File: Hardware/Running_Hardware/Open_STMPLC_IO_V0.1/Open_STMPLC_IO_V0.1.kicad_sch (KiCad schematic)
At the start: 73 parts, among them J1 Screw_Terminal_01x02, J2 Screw_Terminal_01x02, J3 Screw_Terminal_01x02, J4 Screw_Terminal_01x02, J5 Screw_Terminal_01x04, Q1 SUD50P06, Q2 AO3400A, SW1 SW_SPDT, SW2 SW_SPDT, SW3 SW_DIP_x02, SW4 SW_SPDT, U10 MAX31865xTP, U11 MAX31856, U12 6N137, U3 TPS1H200A, U7 TPS26600PWP, U8 UCC23513

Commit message: IO board changes
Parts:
- removed C1: 100nF, symbol Device:C_Small
- removed C10: 620nF, symbol Device:C_Small
- removed C11, C14, C6: 10nF, Capacitor_SMD:C_0603_1608Metric_Pad1.08x0.95mm_HandSolder, symbol Device:C_Small
- removed C12, C13, C15, C4, C5, C7: 100nF, Capacitor_SMD:C_0603_1608Metric_Pad1.08x0.95mm_HandSolder, symbol Device:C_Small
- removed C2: 10uF, symbol Device:C_Small
- removed C8: 1uF, symbol Device:C_Small
- removed C9: 2.2uF, symbol Device:C_Small
- removed D1, D2, D6, D7: SS54, symbol Device:D_Schottky_Small
- removed D10, D3, D5: SMAJ33CA, Diode_SMD:D_SMA, symbol Diode:SMAJ33CA
- removed D4: BZT52C12, symbol Device:D_Zener_Small
- removed FB1, FB2: 120R@100MHz, symbol Device:FerriteBead_Small
- removed J1, J2, J4: Screw_Terminal_01x02, symbol Connector:Screw_Terminal_01x02
- removed J5: Screw_Terminal_01x04, symbol Connector:Screw_Terminal_01x04
- removed Q1: SUD50P06, Package_TO_SOT_SMD:TO-252-3_TabPin2, symbol Transistor_FET:Q_PMOS_GDS
- removed Q2: AO3400A, Package_TO_SOT_SMD:SOT-23, symbol Transistor_FET:AO3400A
- removed R1, R14: 10K, symbol Device:R_Small
- removed R10: 1K, symbol Device:R_Small
- removed R11: 470R, symbol Device:R_Small
- removed R12, R13: 150R, Resistor_SMD:R_0603_1608Metric_Pad0.98x0.95mm_HandSolder, symbol Device:R_Small
- removed R15: 100K, symbol Device:R_Small
- removed R16, R3: 10K, Resistor_SMD:R_0603_1608Metric_Pad0.98x0.95mm_HandSolder, symbol Device:R_Small
- removed R17, R19, R20: 4.7K, Resistor_SMD:R_0603_1608Metric_Pad0.98x0.95mm_HandSolder, symbol Device:R_Small
- removed R18: 15K, symbol Device:R_Small
- removed R2: 47R, symbol Device:R_Small
- removed R21, R23, R24: 2.2K, Resistor_SMD:R_0603_1608Metric_Pad0.98x0.95mm_HandSolder, symbol Device:R_Small
- removed R26: 400R, Resistor_SMD:R_0603_1608Metric_Pad0.98x0.95mm_HandSolder, symbol Device:R_Small
- removed R28: 4K, Resistor_SMD:R_0603_1608Metric_Pad0.98x0.95mm_HandSolder, symbol Device:R_Small
- removed R4: 1K, Resistor_SMD:R_0603_1608Metric_Pad0.98x0.95mm_HandSolder, symbol Device:R_Small
- removed R5: 715K, Resistor_SMD:R_0603_1608Metric_Pad0.98x0.95mm_HandSolder, symbol Device:R_Small
- removed R6: 20K, Resistor_SMD:R_0603_1608Metric_Pad0.98x0.95mm_HandSolder, symbol Device:R_Small
- removed R7: 30.1K, Resistor_SMD:R_0603_1608Metric_Pad0.98x0.95mm_HandSolder, symbol Device:R_Small
- removed R8: 11.8K, Resistor_SMD:R_0603_1608Metric_Pad0.98x0.95mm_HandSolder, symbol Device:R_Small
- removed R9: 33.2K, Resistor_SMD:R_0603_1608Metric_Pad0.98x0.95mm_HandSolder, symbol Device:R_Small
- removed SW1, SW2, SW4: SW_SPDT, symbol Switch:SW_SPDT
- removed SW3: SW_DIP_x02, symbol Switch:SW_DIP_x02
- removed U10: MAX31865xTP, Package_DFN_QFN:TQFN-20-1EP_5x5mm_P0.65mm_EP3.25x3.25mm, symbol Sensor_Temperature:MAX31865xTP
- removed U11: MAX31856, Package_SO:TSSOP-14_4.4x5mm_P0.65mm, symbol Sensor_Temperature:MAX31856
- removed U3: TPS1H200A, Package_SO:HVSSOP-8-1EP_3x3mm_P0.65mm_EP1.57x1.89mm_ThermalVias, symbol TPS1H200A:TPS1H200A
- removed U7: TPS26600PWP, Package_SO:HTSSOP-16-1EP_4.4x5mm_P0.65mm_EP3.4x5mm_Mask2.66x2.46mm_ThermalVias, symbol Power_Management:TPS26600PWP
- removed U8: UCC23513, Package_SO:SSO-6_6.8x4.6mm_P1.27mm_Clearance8mm, symbol UCC23153:UCC23513
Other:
- added sheet DIG_HS_OUT_1 (untitled.kicad_sch)
- added sheet DIG_OUT (DIG_OUT.kicad_sch)
- added sheet Temp_Sensor (Temp_Sensor.kicad_sch)
- note removed: "2/3W"
- note removed: "2/4W"
- note removed: "2W"
- note removed: "3W"
- note removed: "PT100"
- note removed: "PT1000"

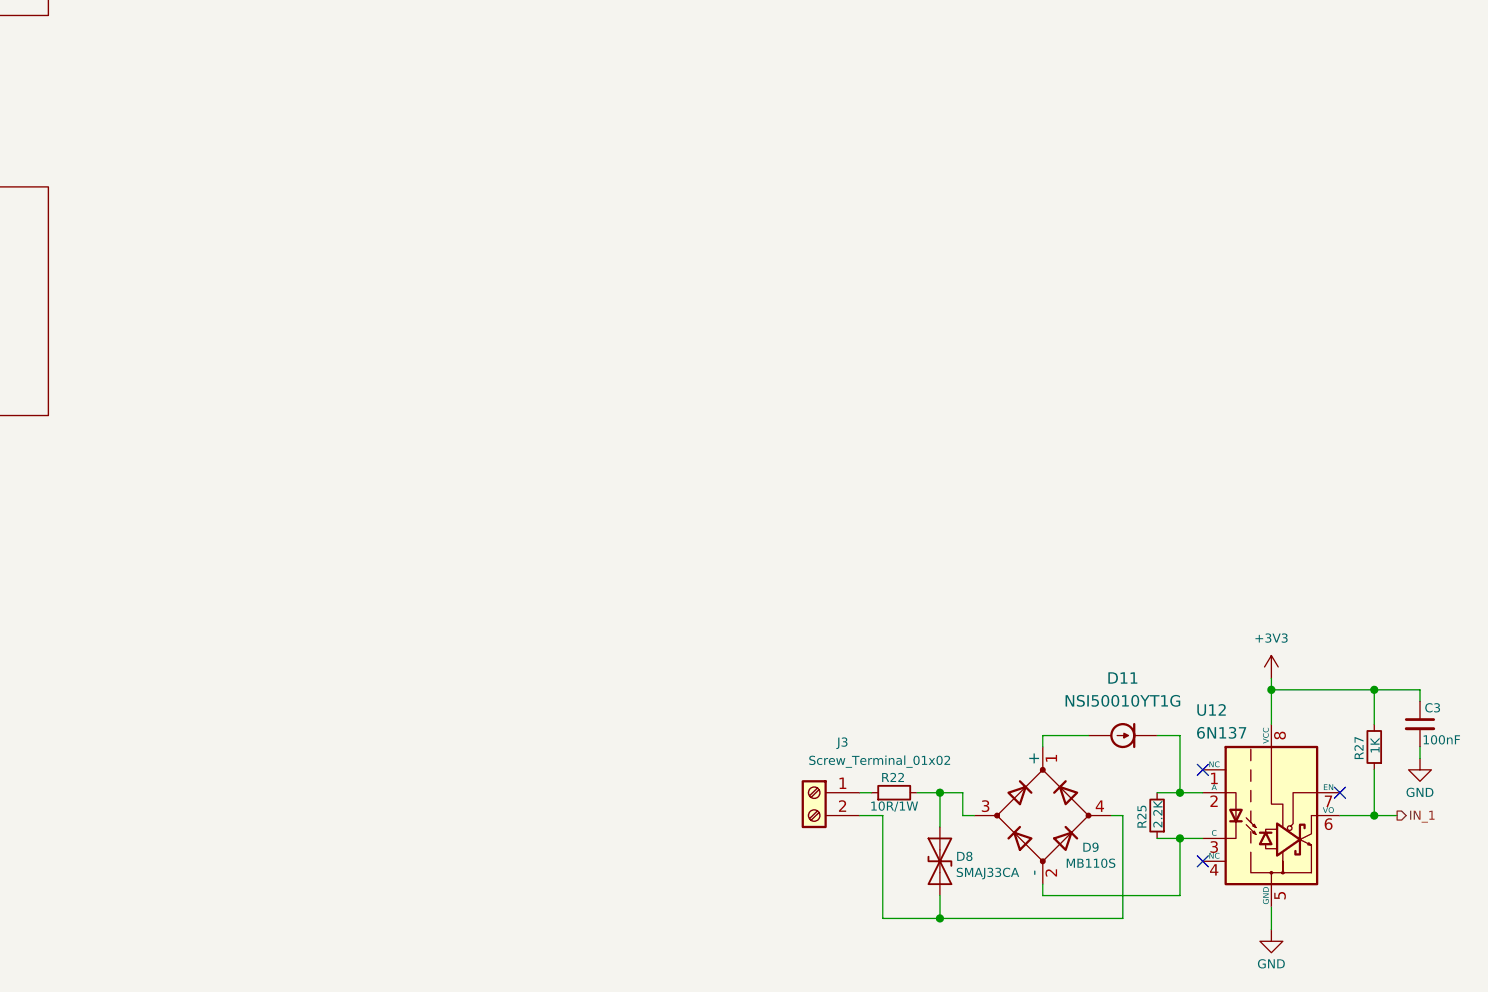
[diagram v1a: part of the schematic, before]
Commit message: IO board schematic changes
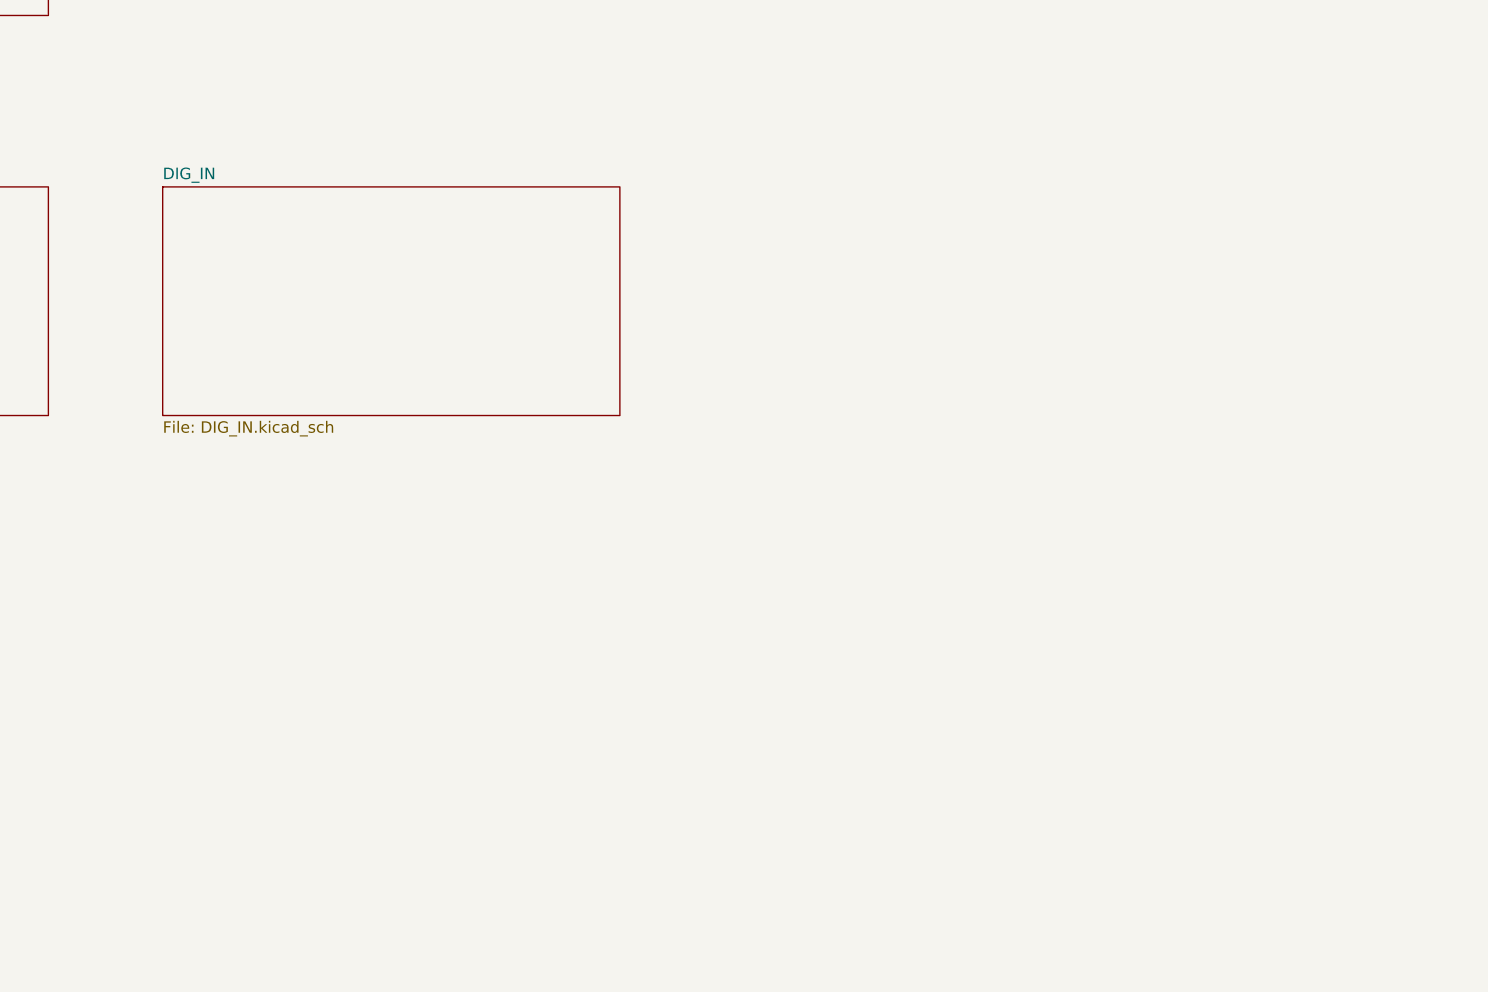
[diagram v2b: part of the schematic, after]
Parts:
- removed C3: 100nF, symbol Device:C_Small
- removed D11: NSI50010YT1G, Diode_SMD:D_SOD-123, symbol Device:D_Current-regulator
- removed D8: SMAJ33CA, Diode_SMD:D_SMA, symbol Diode:SMAJ33CA
- removed D9: MB110S, Package_TO_SOT_SMD:TO-269AA, symbol Device:D_Bridge_+-AA
- removed J3: Screw_Terminal_01x02, symbol Connector:Screw_Terminal_01x02
- removed R22: 10R/1W, Resistor_SMD:R_0603_1608Metric_Pad0.98x0.95mm_HandSolder, symbol Device:R_Small
- removed R25: 2.2K, Resistor_SMD:R_0603_1608Metric_Pad0.98x0.95mm_HandSolder, symbol Device:R_Small
- removed R27: 1K, Resistor_SMD:R_0603_1608Metric_Pad0.98x0.95mm_HandSolder, symbol Device:R_Small
- removed U12: 6N137, Package_DIP:DIP-8_W7.62mm, symbol Isolator:6N137
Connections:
- no-connect marks 3 -> 0
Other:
- added sheet DIG_IN (DIG_IN.kicad_sch)

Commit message: Digital IO completion
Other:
- removed sheet DIG_IN
- added sheet DIG_HS_OUT_2 (DIG_HS_OUT_2.kicad_sch)
- added sheet DIG_HS_OUT_3 (DIG_HS_OUT_3.kicad_sch)
- added sheet DIG_HS_OUT_4 (DIG_HS_OUT_4.kicad_sch)
- added sheet DIG_IN_GRP1 (DIG_IN_GRP1.kicad_sch)
- added sheet DIG_IN_GRP2 (DIG_IN_GRP2.kicad_sch)
- added sheet DIG_IN_GRP3 (DIG_IN_GRP3.kicad_sch)
- sheet DIG_HS_OUT_1: file untitled.kicad_sch -> DIG_HS_OUT_1.kicad_sch

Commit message: Analog out section
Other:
- added sheet ANALOG_IN (ANALOG_IN.kicad_sch)
- added sheet ANALOG_OUT (ANALOG_OUT.kicad_sch)
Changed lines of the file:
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@@
+	)
+	(sheet
+		(at 114.3 170.18)
+		(size 50.8 25.4)
+		(exclude_from_sim no)
+		(in_bom yes)
+		(on_board yes)
+		(dnp no)
+		(stroke
+			(width 0.1524)
+			(type solid)
+		)
+		(fill
+			(color 255 255 194 1.0000)
+		)
+		(property "Sheetname" "ANALOG_IN"
+			(at 114.554 173.99 0)
+			(effects
+				(font
+					(size 2 2)
+					(thickness 0.4)
+					(bold yes)
+				)
+				(justify left bottom)
+			)
+		)
+		(property "Sheetfile" "ANALOG_IN.kicad_sch"
+			(at 114.3 196.1646 0)
+			(effects
+				(font
+					(size 1.27 1.27)
+				)
+				(justify left top)
+			)
+		)
+		(instances
+			(project "Open_STMPLC_IO_V0.1"
+				(path "/4d6787b6-1f4f-4098-b70b-d936e584350b"
+					(page "11")
+				)
+			)
+		)
 	)
 	(sheet
@@
 				)
 			)
+		)
+	)
+	(sheet
+		(at 50.8 170.18)
+		(size 50.8 25.4)
+		(exclude_from_sim no)
+		(in_bom yes)
+		(on_board yes)
+		(dnp no)
+		(stroke
+			(width 0.1524)
+			(type solid)
+		)
+		(fill
+			(color 255 255 194 1.0000)
+		)
+		(property "Sheetname" "ANALOG_OUT"
+			(at 51.054 173.99 0)
+			(effects
+				(font
+					(size 2 2)
+					(thickness 0.4)
+					(bold yes)
+				)
+				(justify left bottom)
+			)
+		)
+		(property "Sheetfile" "ANALOG_OUT.kicad_sch"
+			(at 50.8 196.1646 0)
+			(effects
+				(font
+					(size 1.27 1.27)
+				)
+				(justify left top)
+			)
+		)
+		(instances
+			(project "Open_STMPLC_IO_V0.1"
+				(path "/4d6787b6-1f4f-4098-b70b-d936e584350b"
+					(page "10")
+				)
+			)

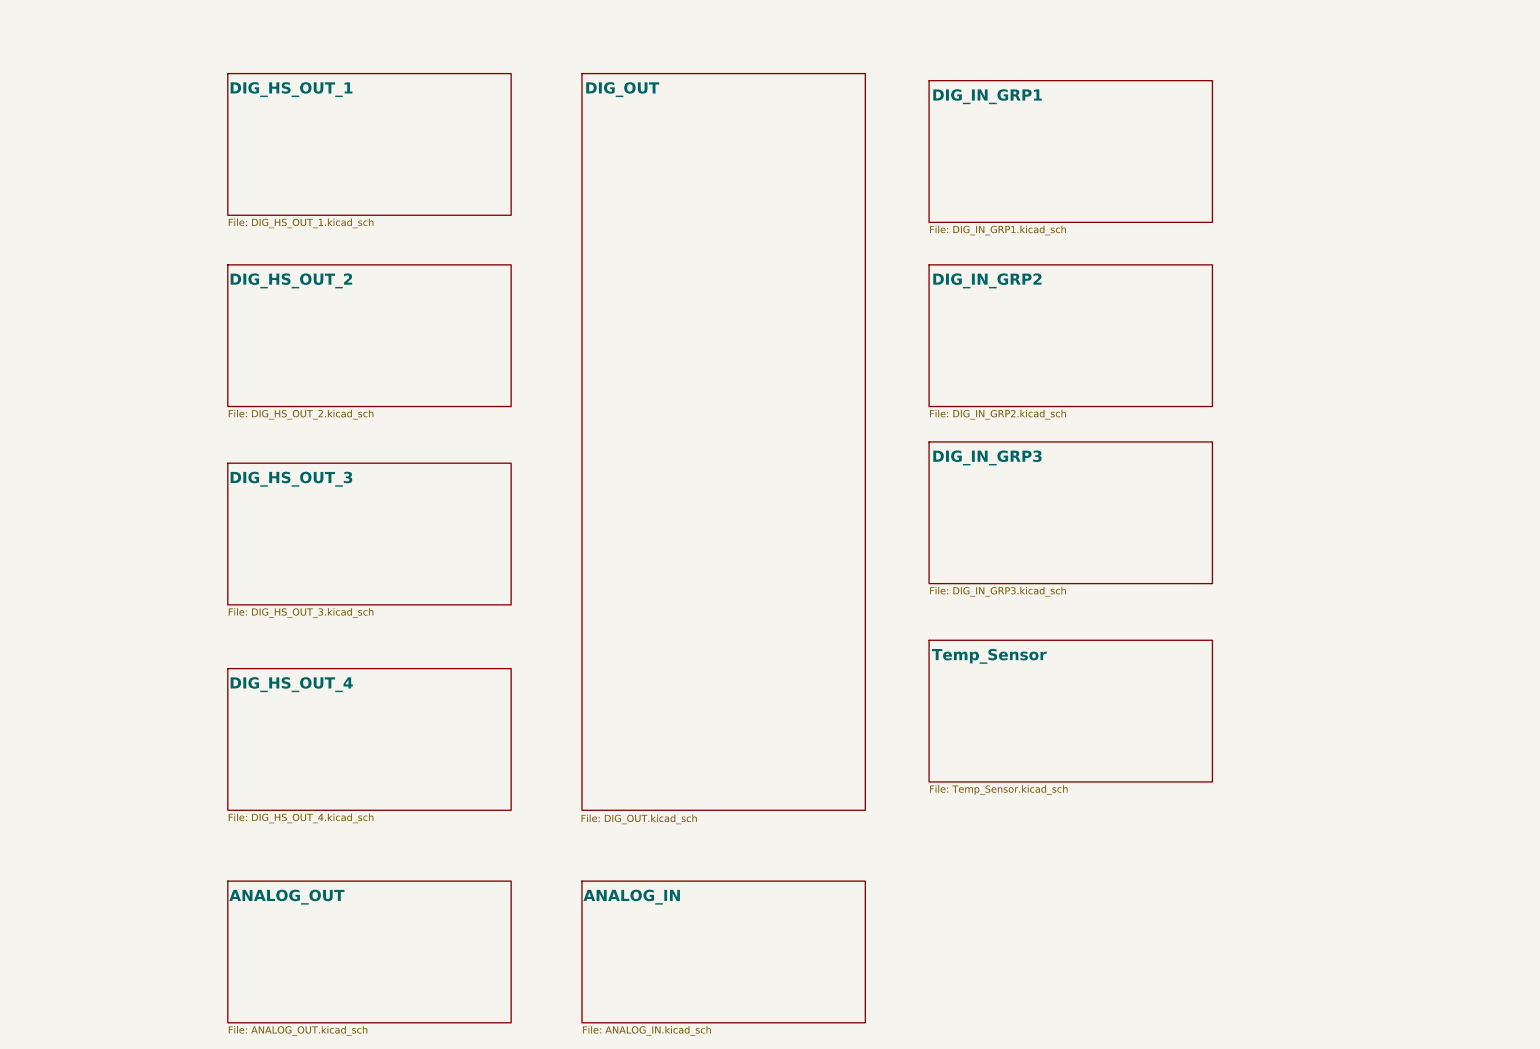
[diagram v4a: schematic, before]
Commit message: GSM Module add
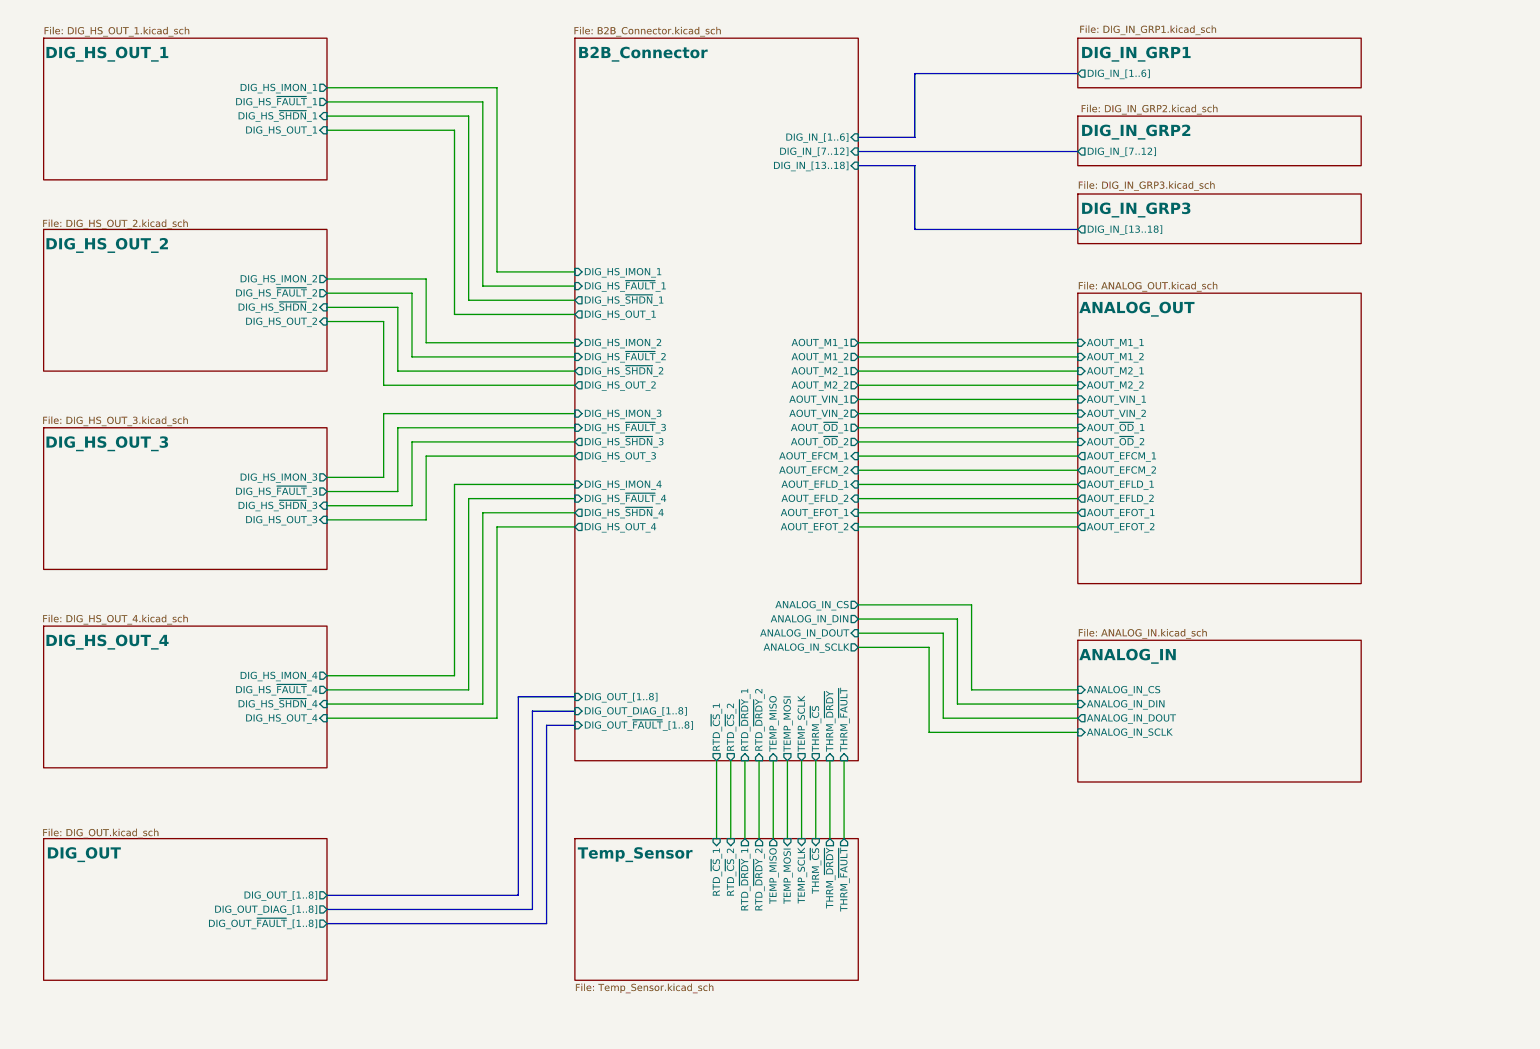
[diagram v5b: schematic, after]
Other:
- added sheet B2B_Connector (B2B_Connector.kicad_sch)
- sheet ANALOG_IN ports: added ANALOG_IN_CS, ANALOG_IN_DIN, ANALOG_IN_DOUT, ANALOG_IN_SCLK; removed none
- sheet ANALOG_OUT ports: added AOUT_EFCM_1, AOUT_EFCM_2, AOUT_EFLD_1, AOUT_EFLD_2, AOUT_EFOT_1, AOUT_EFOT_2, AOUT_M1_1, AOUT_M1_2, AOUT_M2_1, AOUT_M2_2, AOUT_VIN_1, AOUT_VIN_2, AOUT_~{OD}_1, AOUT_~{OD}_2; removed none
- sheet DIG_HS_OUT_1 ports: added DIG_HS_IMON_1, DIG_HS_OUT_1, DIG_HS_~{FAULT}_1, DIG_HS_~{SHDN}_1; removed none
- sheet DIG_HS_OUT_2 ports: added DIG_HS_IMON_2, DIG_HS_OUT_2, DIG_HS_~{FAULT}_2, DIG_HS_~{SHDN}_2; removed none
- sheet DIG_HS_OUT_3 ports: added DIG_HS_IMON_3, DIG_HS_OUT_3, DIG_HS_~{FAULT}_3, DIG_HS_~{SHDN}_3; removed none
- sheet DIG_HS_OUT_4 ports: added DIG_HS_IMON_4, DIG_HS_OUT_4, DIG_HS_~{FAULT}_4, DIG_HS_~{SHDN}_4; removed none
- sheet DIG_IN_GRP1 ports: added DIG_IN_[1..6]; removed none
- sheet DIG_IN_GRP2 ports: added DIG_IN_[7..12]; removed none
- sheet DIG_IN_GRP3 ports: added DIG_IN_[13..18]; removed none
- sheet DIG_OUT ports: added DIG_OUT_DIAG_[1..8], DIG_OUT_[1..8], DIG_OUT_~{FAULT}_[1..8]; removed none
- sheet Temp_Sensor ports: added RTD_~{CS}_1, RTD_~{CS}_2, RTD_~{DRDY}_1, RTD_~{DRDY}_2, TEMP_MISO, TEMP_MOSI, TEMP_SCLK, THRM_~{CS}, THRM_~{DRDY}, THRM_~{FAULT}; removed none
- title: (none) -> Open_PLC_IO
